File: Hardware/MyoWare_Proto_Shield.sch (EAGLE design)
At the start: 24 parts

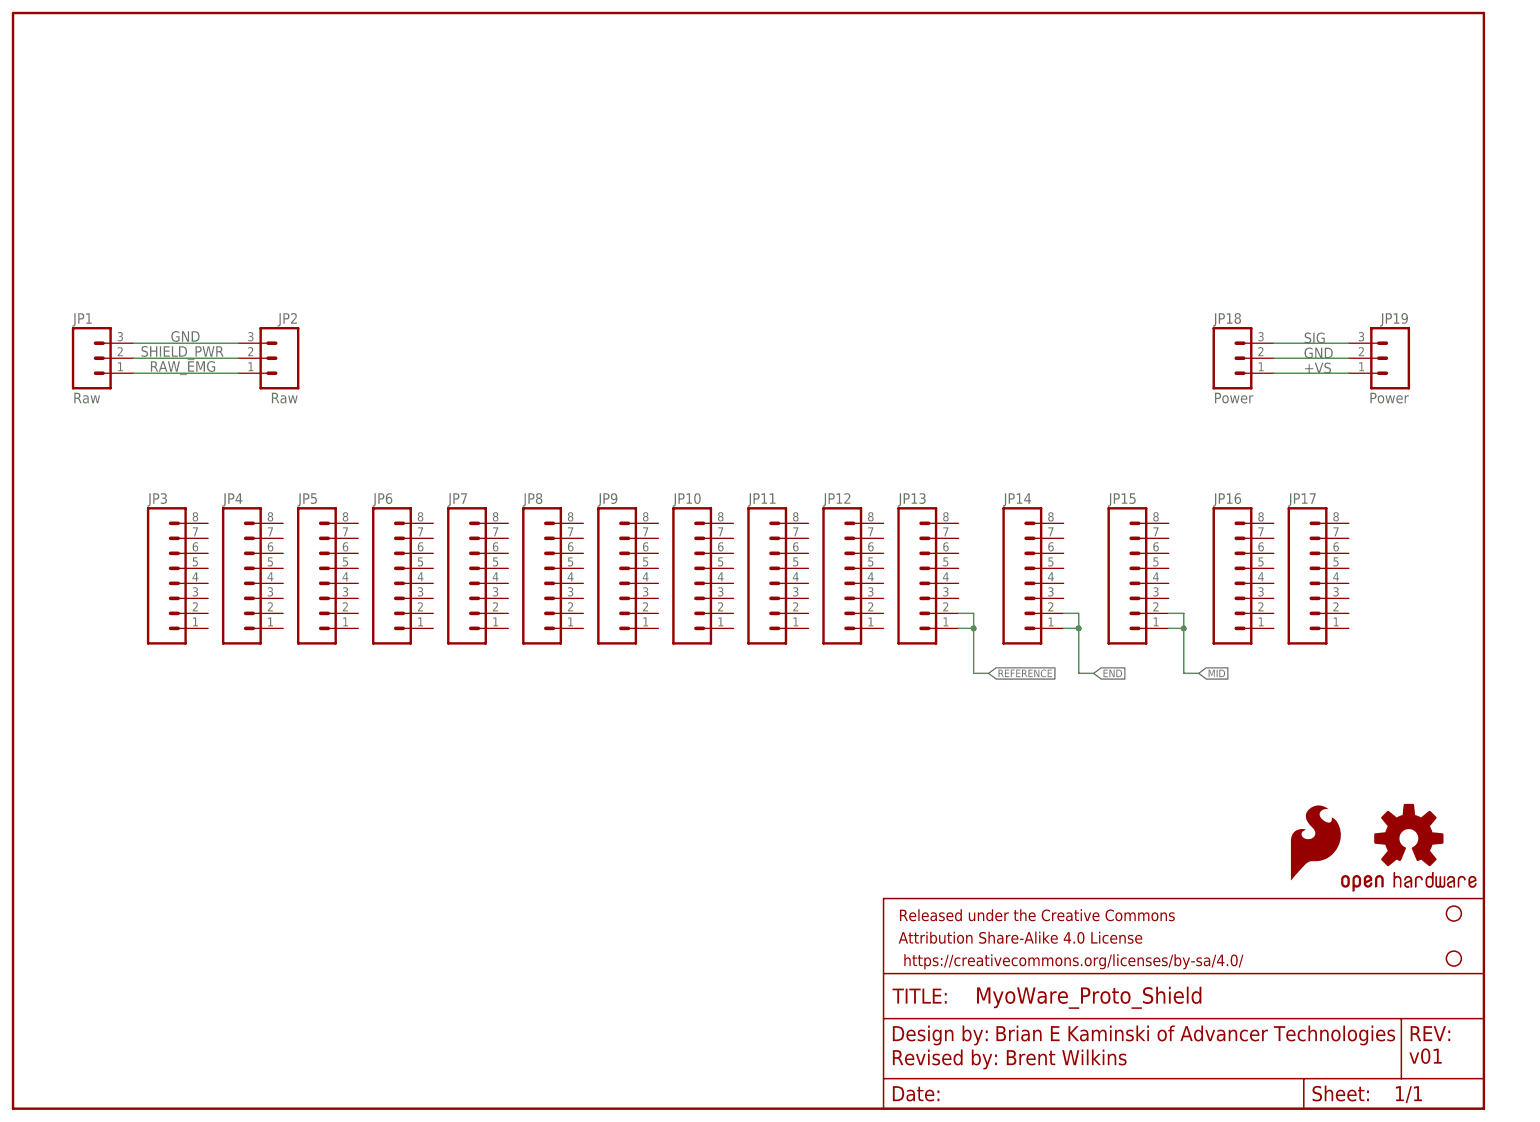
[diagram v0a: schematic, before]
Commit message: Tweaks to meet SFE checklist
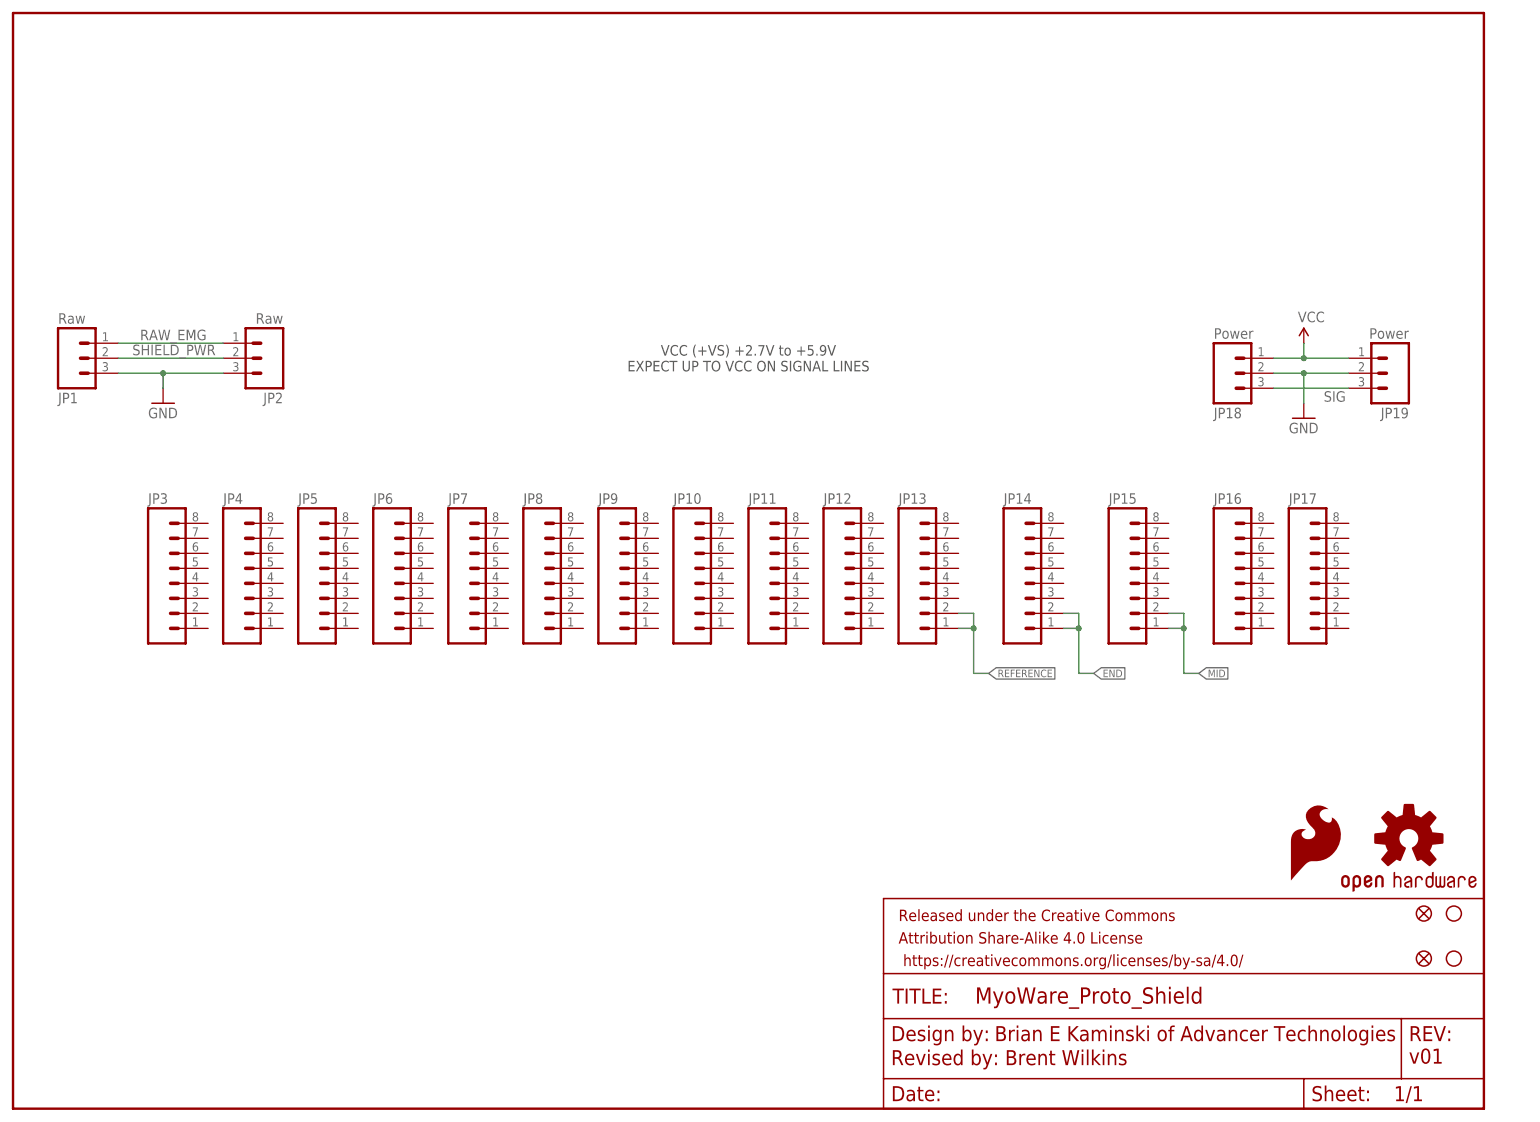
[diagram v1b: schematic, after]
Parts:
- added FID1, FID2: FIDUCIAL1X2, SparkFun-Aesthetics:FIDUCIAL1X2
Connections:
- net +VS renamed VCC
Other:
- note added: "VCC (+VS) +2.7V to +5.9V EXPECT UP TO VCC ON SIGNAL LINES"
- moved on the sheet: JP1, JP18, JP19, JP2

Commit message: Removed fiducials
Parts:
- removed FID1, FID2: FIDUCIAL1X2, SparkFun-Aesthetics:FIDUCIAL1X2
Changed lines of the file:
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@@
 <part name="GND1" library="SparkFun-Aesthetics" deviceset="GND" device=""/>
 <part name="GND2" library="SparkFun-Aesthetics" deviceset="GND" device=""/>
-<part name="FID1" library="SparkFun-Aesthetics" deviceset="FIDUCIAL" device="1X2"/>
-<part name="FID2" library="SparkFun-Aesthetics" deviceset="FIDUCIAL" device="1X2"/>
 </parts>
 <sheets>
@@
 <instance part="GND1" gate="1" x="218.44" y="116.84"/>
 <instance part="GND2" gate="1" x="25.4" y="119.38"/>
-<instance part="FID1" gate="G$1" x="238.76" y="33.02"/>
-<instance part="FID2" gate="G$1" x="238.76" y="25.4"/>
 </instances>
 <busses>

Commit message: Updated version to 10
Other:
- note added: "v10"
- note removed: "v01"
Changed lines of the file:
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@@
 <?xml version="1.0" encoding="utf-8"?>
 <!DOCTYPE eagle SYSTEM "eagle.dtd">
-<eagle version="7.3.1">
+<eagle version="7.3.2">
 <drawing>
 <settings>
@@
 <text x="166.116" y="11.43" size="2.54" layer="94">Brian E Kaminski of Advancer Technologies</text>
 <text x="148.59" y="7.366" size="2.54" layer="94" ratio="10">Revised by: Brent Wilkins</text>
-<text x="236.22" y="7.62" size="2.54" layer="94" font="vector">v01</text>
+<text x="236.22" y="7.62" size="2.54" layer="94" font="vector">v10</text>
 <text x="124.46" y="127" size="1.778" layer="97" font="vector" ratio="15" align="center">VCC (+VS) +2.7V to +5.9V
 EXPECT UP TO VCC ON SIGNAL LINES</text>
